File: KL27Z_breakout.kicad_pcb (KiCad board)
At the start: 2 copper layers, 11.2 x 47.6 mm, 14 parts, among them J1 USB_mini_micro_B, P1 CONN_01X06, P2 CONN_01X08, P3 CONN_01X08, P4 CONN_01X06, SW1 SW_PUSH, SW2 SW_PUSH, U1 MKL27Z256VFM4

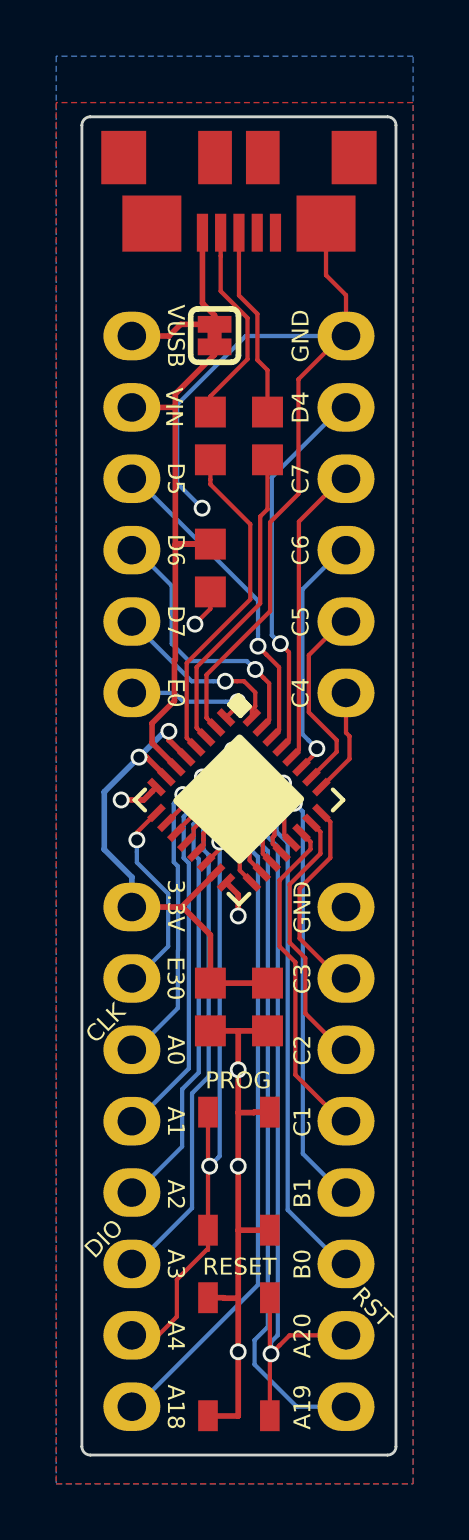
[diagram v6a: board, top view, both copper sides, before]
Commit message: Shorten board size
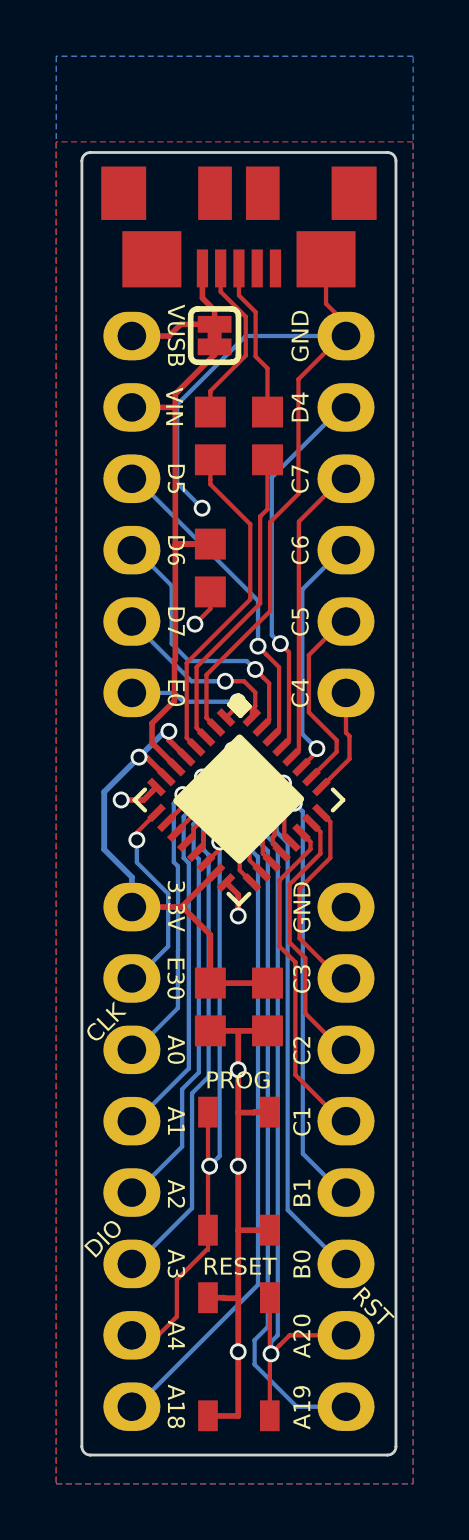
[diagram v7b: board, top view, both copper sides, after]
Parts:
- moved J1 1.27 mm to (103.8, 97.5)
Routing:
- net Net-(J1-Pad2): track 7.32 -> 6.00 mm
- net Net-(J1-Pad3): track 6.80 -> 5.53 mm
- net VBUS: track 6.55 -> 5.28 mm
- net GND: track 55.9 -> 54.7 mm
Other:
- board size 11.2 x 47.6 mm -> 11.2 x 46.4 mm
- board text added: "Rev.B"
